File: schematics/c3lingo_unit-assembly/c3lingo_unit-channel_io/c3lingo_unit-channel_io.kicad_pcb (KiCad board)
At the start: 2 copper layers, 75 x 45 mm, 40 parts, among them J601 Mic X In, J602 Headphone X, J603 Interconnect, J604 PowerSupply, U601 NE5534, U602 TPA6111A2

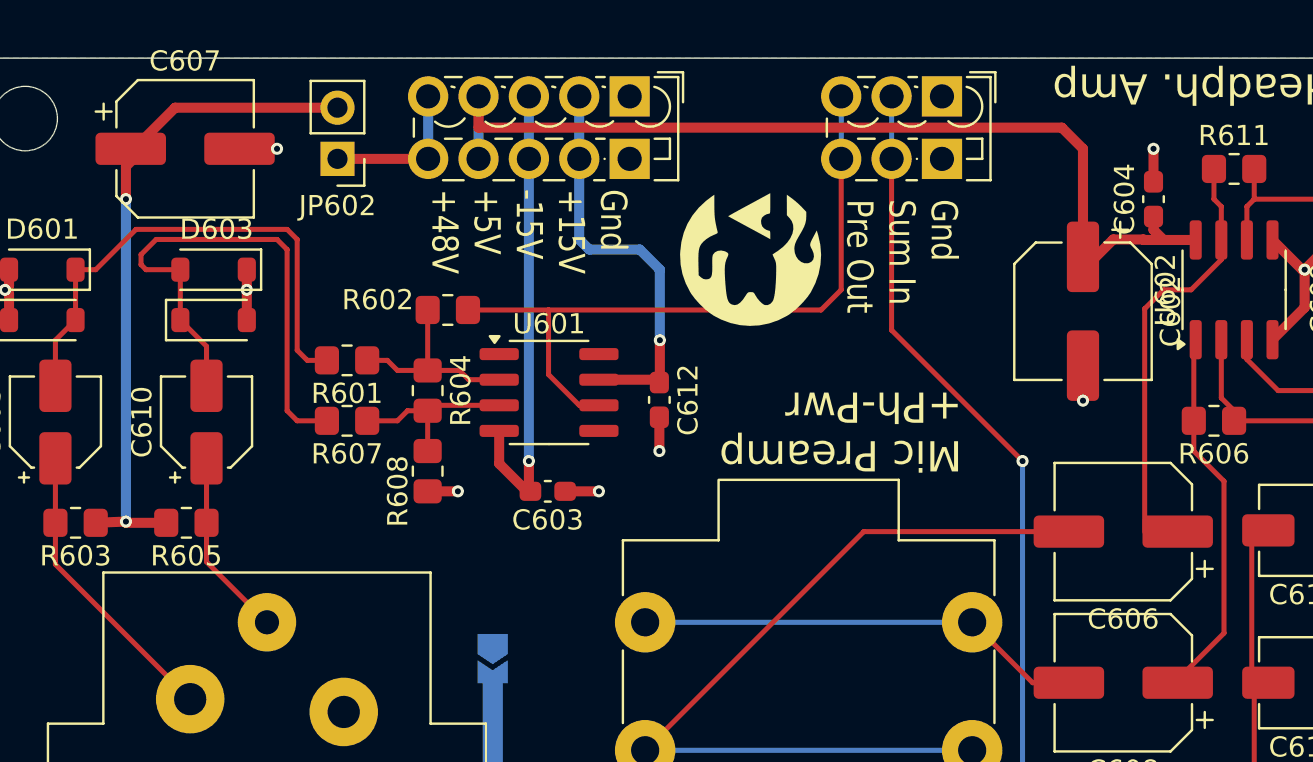
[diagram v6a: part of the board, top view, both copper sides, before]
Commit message: Channel: Change to single channel potentiometers
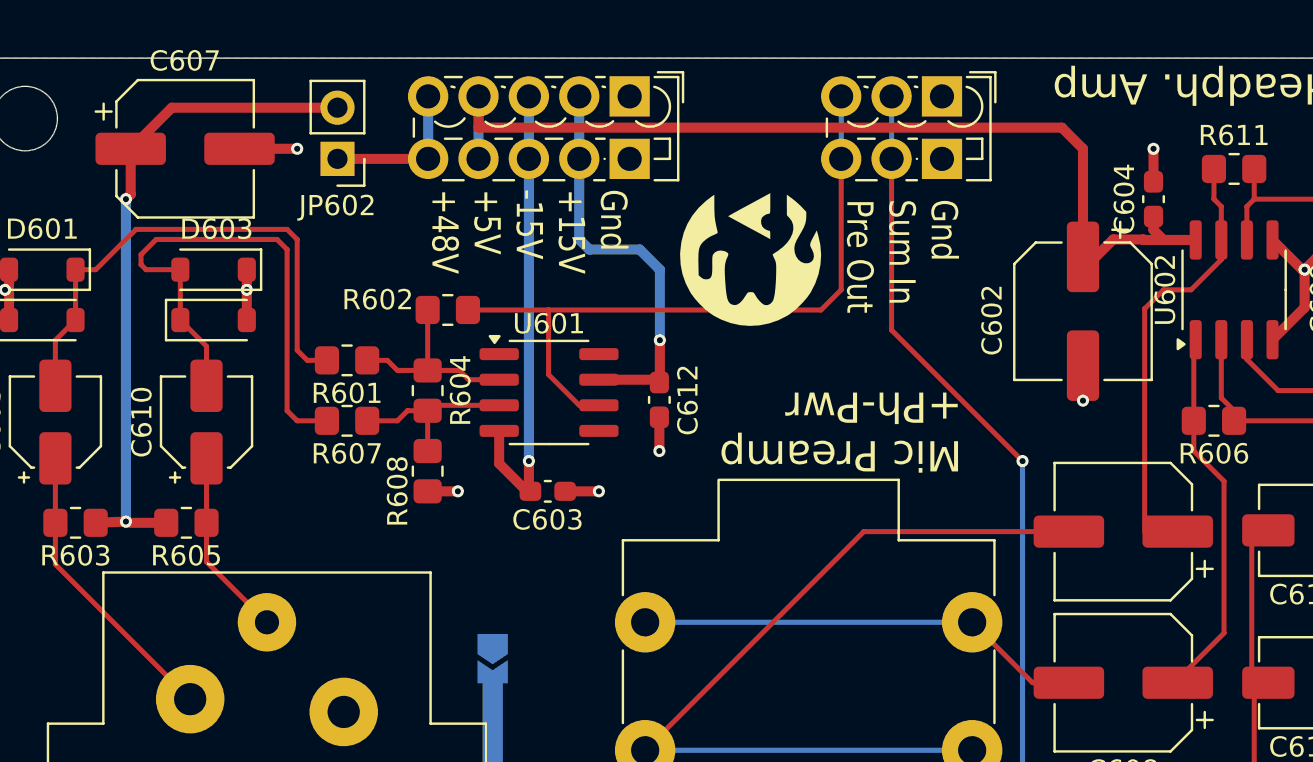
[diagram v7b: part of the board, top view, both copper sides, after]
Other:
- board text added: "c3lingo Interpreter Unit Channel I/O v0.3.2 2024-09-06"
- board text removed: "c3lingo Interpreter Unit Channel I/O v0.3.1 2024-08-30"
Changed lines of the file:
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@@
 	(title_block
 		(title "c3lingo interpeter unit -- channel strip")
-		(date "2024-08-30")
-		(rev "v0.3.1")
+		(date "2024-09-06")
+		(rev "v0.3.2")
 		(company "Jannik Beyerstedt (jtbx)")
 		(comment 1 "Prototype 2")
@@
 			(drillshape 0)
 			(scaleselection 1)
-			(outputdirectory "c3lingo_unit-channel-gerber")
+			(outputdirectory "c3lingo_unit-channel_io-gerber")
 		)
 	)
@@
 		(tags "capacitor electrolytic")
 		(property "Reference" "C602"
-			(at 0 -4.35 -90)
+			(at 0.4375 4.5 -90)
 			(layer "F.SilkS")
 			(effects
@@
 			(at 0 -4.35 180)
 			(layer "F.SilkS")
+			(hide yes)
 			(effects
 				(font
@@
 		(layer "Edge.Cuts")
 	)
-	(gr_text "c3lingo Interpreter Unit\nChannel I/O\nv0.3.1 2024-08-30"
+	(gr_text "c3lingo Interpreter Unit\nChannel I/O\nv0.3.2 2024-09-06"
 		(at 88.5 164.5 180)
 		(layer "B.SilkS")
@@
 	)
 	(segment
-		(start 63 159.5)
-		(end 65.5 159.5)
-		(width 0.5)
-		(layer "F.Cu")
-		(net 3)
-	)
-	(segment
 		(start 79.975 176.5)
 		(end 81.475 176.5)
@@
 		(net 3)
 	)
+	(segment
+		(start 63.6375 159.5)
+		(end 66.5 159.5)
+		(width 0.5)
+		(layer "F.Cu")
+		(net 3)
+	)
 	(via
 		(at 74.475 176.5)
@@
 	)
 	(via
-		(at 65.5 159.5)
+		(at 105.5 172)
 		(size 0.6)
 		(drill 0.3)
@@
 	)
 	(via
-		(at 105.5 172)
+		(at 84.475 174.5)
 		(size 0.6)
 		(drill 0.3)
@@
 	)
 	(via
-		(at 84.475 174.5)
+		(at 64 166.5)
 		(size 0.6)
 		(drill 0.3)
@@
 	)
 	(via
-		(at 64 166.5)
+		(at 81.475 176.5)
 		(size 0.6)
 		(drill 0.3)
@@
 	)
 	(via
-		(at 81.475 176.5)
+		(at 66.5 159.5)
 		(size 0.6)
 		(drill 0.3)
@@
 	)
 	(segment
-		(start 58 162)
-		(end 58 160.375)
+		(start 58.2375 159.5)
+		(end 58.2375 161.7625)
 		(width 0.5)
 		(layer "F.Cu")
@@
 	)
 	(segment
-		(start 60.44 157.46)
-		(end 58.4 159.5)
+		(start 60.2775 157.46)
+		(end 58.2375 159.5)
 		(width 0.5)
 		(layer "F.Cu")
@@
 	)
 	(segment
-		(start 58 160.375)
-		(end 58.875 159.5)
+		(start 68.5 157.46)
+		(end 60.2775 157.46)
 		(width 0.5)
 		(layer "F.Cu")
@@
 	)
 	(segment
-		(start 68.5 157.46)
-		(end 60.44 157.46)
+		(start 58 178.0625)
+		(end 60 178.0625)
 		(width 0.5)
 		(layer "F.Cu")
@@
 	)
 	(segment
-		(start 58 178.0625)
-		(end 60 178.0625)
+		(start 58.2375 161.7625)
+		(end 58 162)
 		(width 0.5)
 		(layer "F.Cu")

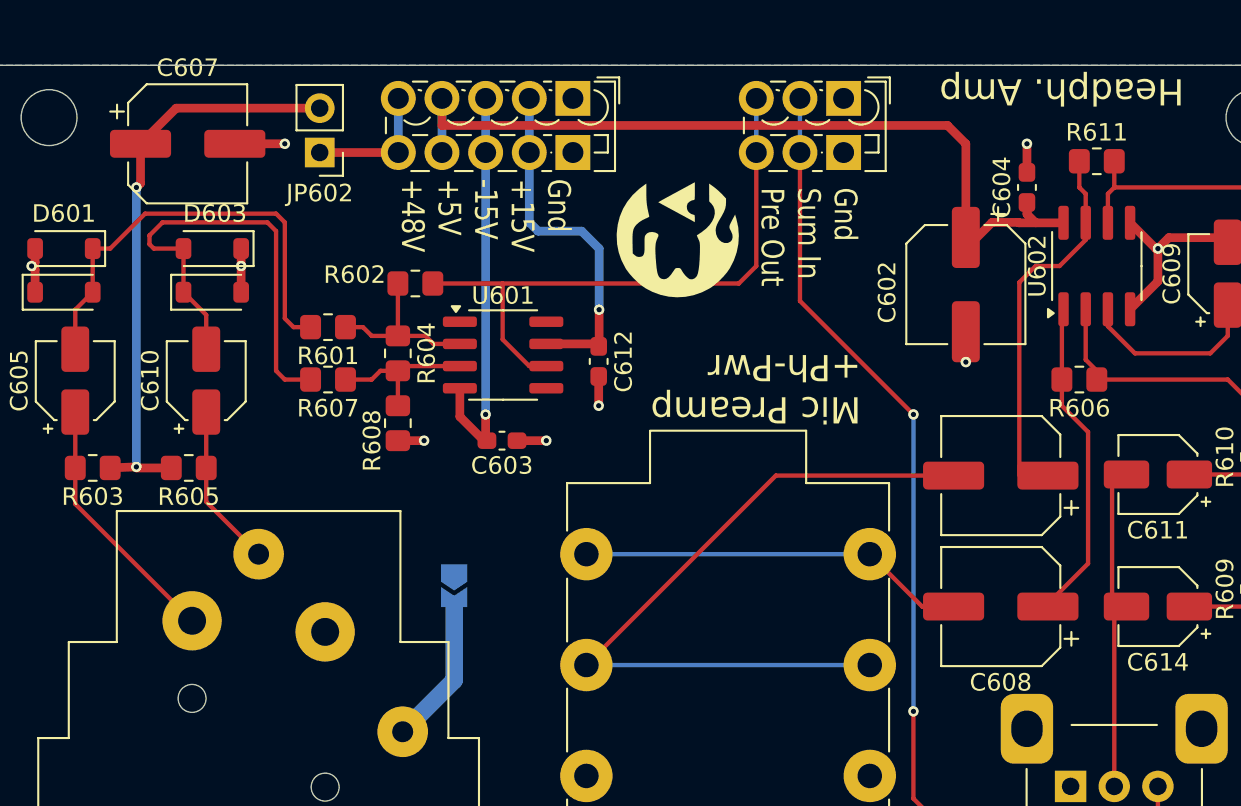
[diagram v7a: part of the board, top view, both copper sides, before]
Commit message: Move potentiometers down, fix JLC PCB components
- Fix JLC PCB component orientation
- Add do-not-populate to all THD components
- Fix JLC part selection, tweak values to be standard components
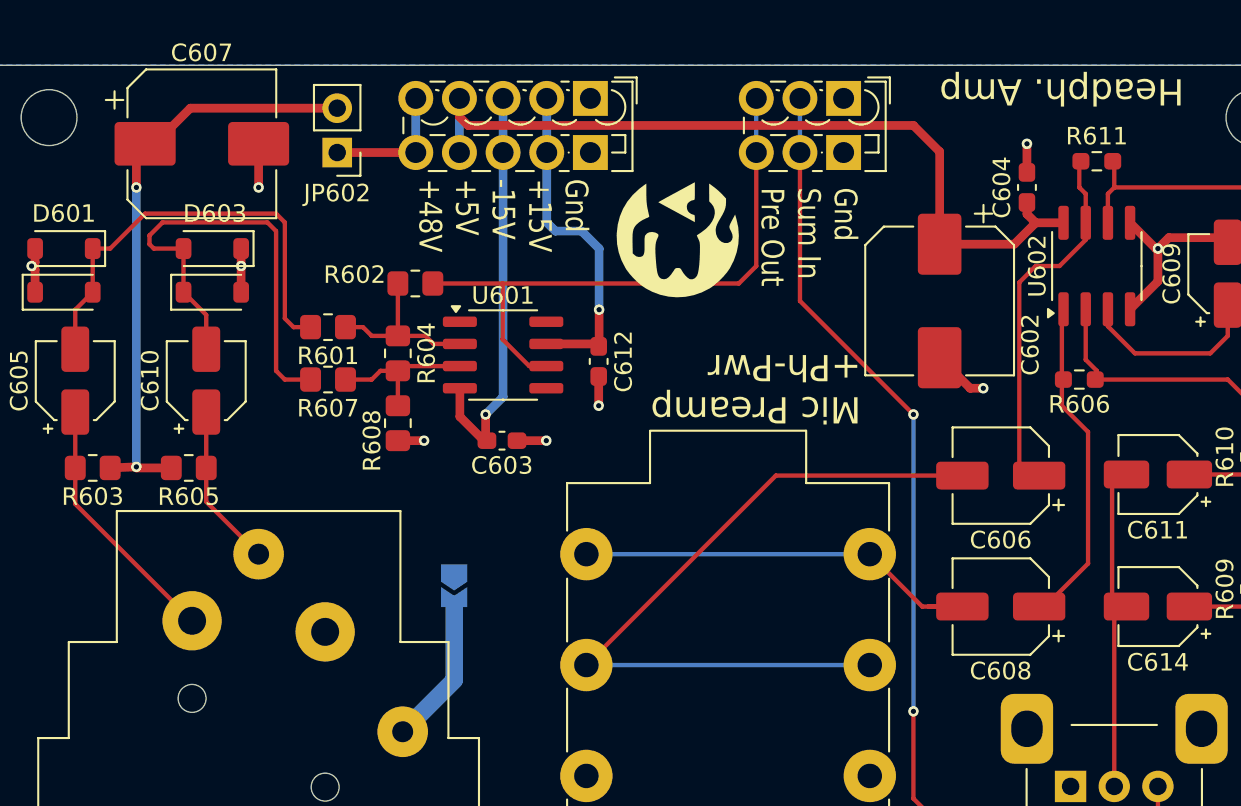
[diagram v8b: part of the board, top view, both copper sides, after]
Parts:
- C602: footprint Capacitor_SMD:CP_Elec_6.3x7.7 -> Capacitor_SMD:CP_Elec_8x10
- C606, C608: footprint Capacitor_SMD:CP_Elec_6.3x5.8 -> Capacitor_SMD:CP_Elec_5x5.8
- C607: value 100uF/ 63V -> 100uF/ 50V; footprint Capacitor_SMD:CP_Elec_6.3x7.7 -> Capacitor_SMD:CP_Elec_8x10
- R606, R611: footprint Resistor_SMD:R_0805_2012Metric_Pad1.20x1.40mm_HandSolder -> Resistor_SMD:R_0603_1608Metric_Pad0.98x0.95mm_HandSolder
- moved C602 1.77 mm to (104.0, 168.5)
- moved J604 1.00 mm to (84.0, 156.9)
- moved JP602 1.00 mm to (69.5, 160.0)
- moved C607 0.81 mm to (61.8, 159.5)
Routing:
- net +5V: track 48.7 -> 46.8 mm
- net +15V: track 20.2 -> 19.2 mm
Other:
- board text added: "c3lingo Interpreter Unit Channel I/O v0.3.3 2024-09-08"
- board text removed: "c3lingo Interpreter Unit Channel I/O v0.3.2 2024-09-06"
